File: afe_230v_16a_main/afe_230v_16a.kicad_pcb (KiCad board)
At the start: 2 copper layers, 67.7 x 86.4 mm, 1 part

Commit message: began PCBA layout
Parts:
- removed REF**: BlackPill, STM-32:YAAJ_BlackPill_SWD_1
- added C1: 1nF, Capacitor_SMD:C_0402_1005Metric, F.Cu at (157.5, 113.8)
- added C2: 1nF, Capacitor_SMD:C_0402_1005Metric, F.Cu at (173.7, 113.8)
- added D1: PDZ36B, Diode_SMD:D_SOD-323F, F.Cu at (124.4, 73.0)
- added D2: PDZ36B, Diode_SMD:D_SOD-323F, F.Cu at (121.4, 73.0)
- added D3: PDZ36B, Diode_SMD:D_SOD-323F, F.Cu at (124.9, 78.2)
- added D4: PDZ36B, Diode_SMD:D_SOD-323F, F.Cu at (121.9, 78.2)
- added J1: ~, Connector_Phoenix_MSTB:PhoenixContact_MSTBVA_2,5_2-G-5,08_1x02_P5.08mm_Vertical, F.Cu at (158.5, 134.4)
- added J2: ~, Connector_Phoenix_MSTB:PhoenixContact_MSTBVA_2,5_2-G-5,08_1x02_P5.08mm_Vertical, F.Cu at (122.6, 134.2)
- added J3: ~, Connector_Phoenix_MSTB:PhoenixContact_MSTBVA_2,5_2-G-5,08_1x02_P5.08mm_Vertical, F.Cu at (138.8, 134.0)
- added J4: MCV 1,5/ 6-G-3,81, Connector_Phoenix_MC:PhoenixContact_MCV_1,5_6-G-3.81_1x06_P3.81mm_Vertical, F.Cu at (159.7, 57.0)
- added J5: HBUS16, Connector_PinHeader_2.54mm:PinHeader_2x09_P2.54mm_Vertical, F.Cu at (119.5, 84.3)
- added R1: 680K, Resistor_SMD:R_1206_3216Metric, F.Cu at (155.4, 124.0)
- added R10: 680K, Resistor_SMD:R_1206_3216Metric, F.Cu at (176.9, 120.3)
- added R11: 680K, Resistor_SMD:R_1206_3216Metric, F.Cu at (155.4, 120.2)
- added R12: 680K, Resistor_SMD:R_1206_3216Metric, F.Cu at (171.8, 120.3)
- added R13: 499K, Resistor_SMD:R_0805_2012Metric, F.Cu at (154.8, 118.0)
- added R14: 499K, Resistor_SMD:R_0805_2012Metric, F.Cu at (171.2, 117.8)
- added R15: 20K, Resistor_SMD:R_0805_2012Metric, F.Cu at (154.4, 115.0)
- added R16: 20K, Resistor_SMD:R_0805_2012Metric, F.Cu at (170.8, 115.0)
- added R17: 20K, Resistor_SMD:R_0805_2012Metric, F.Cu at (157.5, 115.8)
- added R18: 20K, Resistor_SMD:R_0805_2012Metric, F.Cu at (173.8, 115.7)
- added R19: 0K, Resistor_SMD:R_0805_2012Metric, F.Cu at (161.7, 110.8)
- added R2: 680K, Resistor_SMD:R_1206_3216Metric, F.Cu at (171.9, 124.0)
- added R20: 1K_dnp, Resistor_SMD:R_0805_2012Metric, F.Cu at (166.3, 112.0)
- added R21: 0K, Resistor_SMD:R_0805_2012Metric, F.Cu at (178.2, 110.9)
- added R22: 33R2, Resistor_SMD:R_0805_2012Metric, F.Cu at (153.8, 108.7)
- added R23: 33R2, Resistor_SMD:R_0805_2012Metric, F.Cu at (170.3, 108.8)
- added R24: 1K_dnp, Resistor_SMD:R_0805_2012Metric, F.Cu at (163.6, 103.8)
- added R25: 1K_dnp, Resistor_SMD:R_0805_2012Metric, F.Cu at (165.8, 103.8)
- added R26: 1K_dnp, Resistor_SMD:R_0805_2012Metric, F.Cu at (170.6, 99.6)
- added R27: 1K_dnp, Resistor_SMD:R_0805_2012Metric, F.Cu at (159.2, 103.7)
- added R28: 1K_dnp, Resistor_SMD:R_0805_2012Metric, F.Cu at (159.2, 99.6)
- added R29: 0R005, Resistor_SMD:R_2512_6332Metric_Pad1.40x3.35mm_HandSolder, F.Cu at (141.4, 123.4)
- added R3: 680K, Resistor_SMD:R_1206_3216Metric, F.Cu at (160.5, 124.0)
- added R30: 1KR, Resistor_SMD:R_0805_2012Metric, F.Cu at (135.1, 115.3)
- added R31: 1KR, Resistor_SMD:R_0805_2012Metric, F.Cu at (146.5, 115.3)
- added R32: 1KR, Resistor_SMD:R_0805_2012Metric, F.Cu at (135.1, 111.5)
- added R33: 1KR, Resistor_SMD:R_0805_2012Metric, F.Cu at (146.5, 110.8)
- added R34: 1KR, Resistor_SMD:R_0805_2012Metric, F.Cu at (146.4, 106.3)
- added R35: 20K, Resistor_SMD:R_0805_2012Metric, F.Cu at (139.2, 97.8)
- added R36: 20K, Resistor_SMD:R_0805_2012Metric, F.Cu at (142.8, 97.8)
- added R37: 1KR, Resistor_SMD:R_0805_2012Metric, F.Cu at (147.1, 103.4)
- added R38: 0K_dnp, Resistor_SMD:R_0805_2012Metric, F.Cu at (144.0, 102.7)
- added R4: 680K, Resistor_SMD:R_1206_3216Metric, F.Cu at (176.9, 124.0)
- added R5: 680K, Resistor_SMD:R_1206_3216Metric, F.Cu at (165.6, 124.0)
- added R6: 680K, Resistor_SMD:R_1206_3216Metric, F.Cu at (182.0, 124.1)
- added R7: 680K, Resistor_SMD:R_1206_3216Metric, F.Cu at (165.5, 120.3)
- added R8: 680K, Resistor_SMD:R_1206_3216Metric, F.Cu at (182.0, 120.3)
- added R9: 680K, Resistor_SMD:R_1206_3216Metric, F.Cu at (160.5, 120.2)
- added U1: ~, Package_TO_SOT_SMD:TSOT-23-5, F.Cu at (157.5, 110.8)
- added U2: AD8538, Package_TO_SOT_SMD:TSOT-23-5, F.Cu at (174.2, 110.9)
- added U3: AD8538_dnp, Package_TO_SOT_SMD:TSOT-23-5, F.Cu at (164.7, 99.8)
- added U4: AQH3223A, Package_SO:SSO-7-8_6.4x9.78mm_P2.54mm, F.Cu at (125.5, 119.7)
- added U5: ACS711xLCTR-25AB, Package_SO:SOIC-8_3.9x4.9mm_P1.27mm, F.Cu at (141.2, 115.0)
- added U6: AD8538_dnp, Package_TO_SOT_SMD:TSOT-23-5, F.Cu at (140.5, 108.5)
- added U7: REF3030, Package_TO_SOT_SMD:SOT-23, F.Cu at (135.2, 103.9)
- added U9: YAAJ_BlackPill, STM-32:YAAJ_BlackPill_SWD_2, F.Cu at (90.1, 76.5)
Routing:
- net (no net): vias 0 -> 10

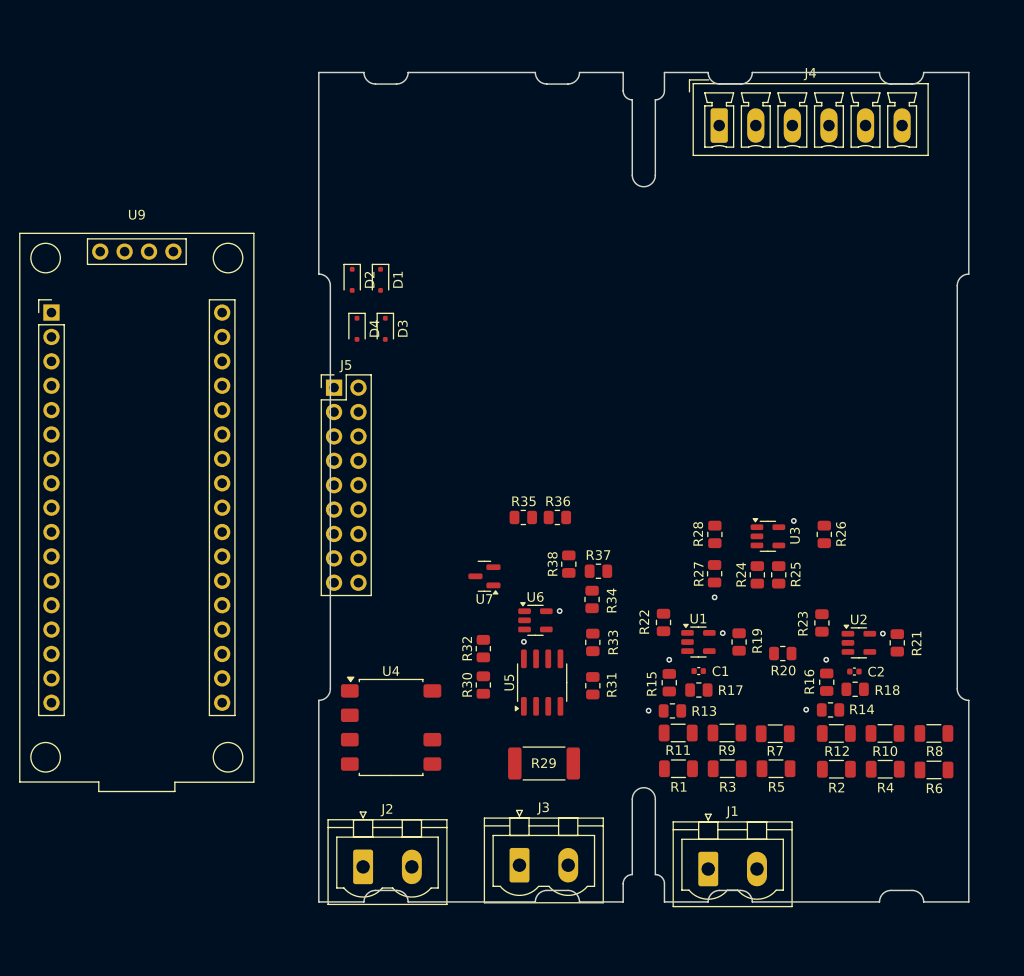
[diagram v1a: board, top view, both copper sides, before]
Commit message: alternate layout
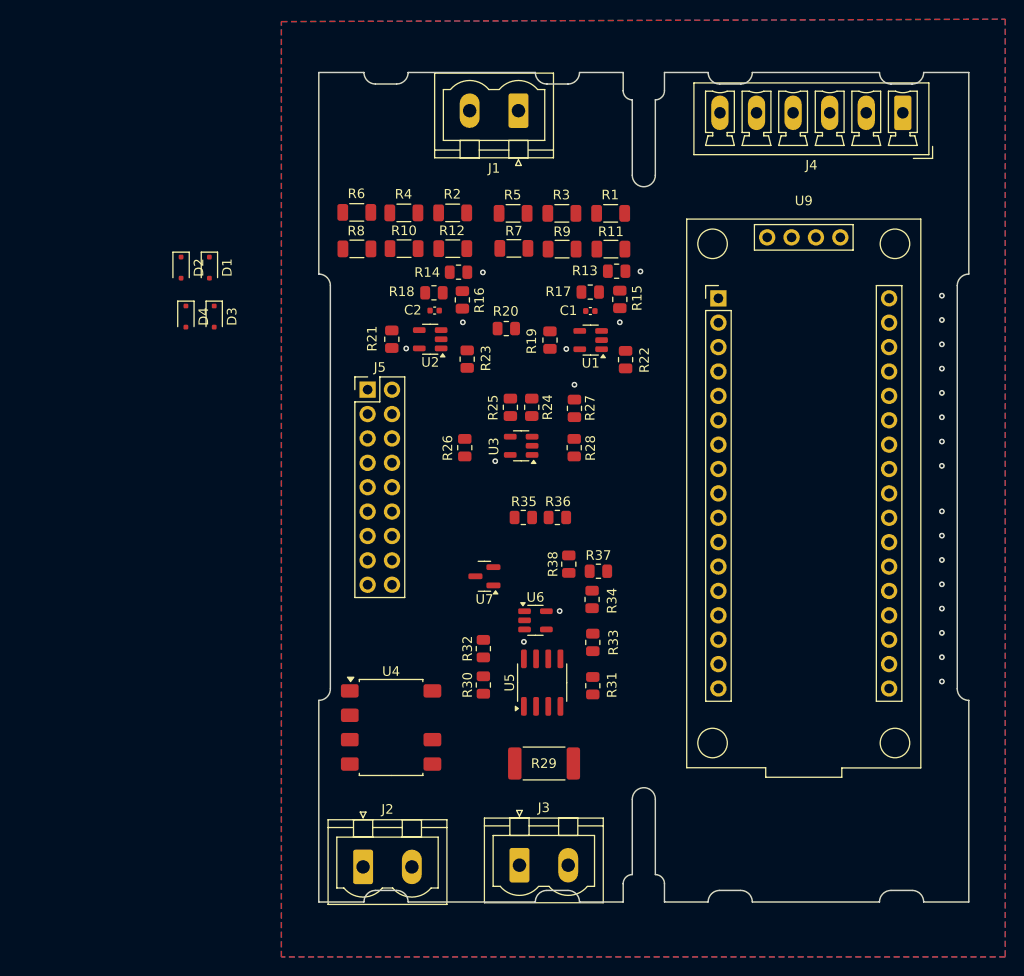
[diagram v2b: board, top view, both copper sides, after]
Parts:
- moved R6 83.6 mm to (121.9, 66.0), turned to 180 degrees
- moved J1 81.4 mm to (138.7, 55.4), turned to 180 degrees
- moved R8 78.5 mm to (121.9, 69.8), turned to 0 degrees
- moved R4 76.6 mm to (126.8, 66.1), turned to 180 degrees
- moved R10 71.1 mm to (126.8, 69.8), turned to 0 degrees
- moved R2 70.4 mm to (131.9, 66.1), turned to 180 degrees
- moved U9 69.5 mm to (159.6, 75.0)
- moved R12 64.4 mm to (131.9, 69.8), turned to 0 degrees
- moved R5 64.0 mm to (138.2, 66.1), turned to 180 degrees
- moved R21 61.4 mm to (125.5, 79.2), turned to 90 degrees
- moved R3 60.4 mm to (143.3, 66.1), turned to 180 degrees
- moved R18 60.3 mm to (129.9, 74.4), turned to 0 degrees
- moved R14 59.8 mm to (132.5, 72.2), turned to 180 degrees
- moved R1 58.3 mm to (148.3, 66.1), turned to 180 degrees
- moved C2 57.7 mm to (130.0, 76.2), turned to 180 degrees
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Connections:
- J5 pad 10: /K1_on -> unconnected-(J5-Pin_10-Pad10)
- J5 pad 11: /CAN_lo -> /CAN_hi
- J5 pad 12: /K1_status -> /K1_on
- J5 pad 13: /24V -> /CAN_lo
- J5 pad 14: /K2_on -> /K1_status
- J5 pad 15: /DGND -> /24V
- J5 pad 16: /K2_status -> /K2_on
- J5 pad 17: (no net) -> /DGND
- J5 pad 18: (no net) -> /K2_status
- J5 pad 9: /CAN_hi -> unconnected-(J5-Pin_9-Pad9)
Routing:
- net Earth: vias 0 -> 16
- added copper zone on B.Cu, net Earth
- added copper zone on F.Cu, net Earth
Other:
- board text added: "I p/n"
- board text added: "K i/o"
- board text added: "V p/n"
- board text added: "blackpill i/o"
- board text added: "outputs & pwr/gnd in"

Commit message: added pcb2&3 board outlines, adjusted i/o
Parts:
- added J6: pinheader_1x6, Connector_PinHeader_2.54mm:PinHeader_1x06_P2.54mm_Vertical, F.Cu at (164.0, 132.4)
- added J6: pinheader_1x6, Connector_PinHeader_2.54mm:PinHeader_1x06_P2.54mm_Vertical, F.Cu at (166.7, 80.8)
- added J6: pinheader_1x6, Connector_PinHeader_2.54mm:PinHeader_1x06_P2.54mm_Vertical, F.Cu at (247.8, 87.5)
- D1, D2, D3, D4: footprint Diode_SMD:D_SOD-323F -> Diode_SMD:D_SOD-323_HandSoldering
- moved J2 90.7 mm to (167.7, 55.5)
- moved J1 79.8 mm to (124.9, 134.0), turned to 0 degrees
- moved U9 68.0 mm to (214.7, 114.9), turned to 90 degrees
- moved U4 67.8 mm to (171.3, 69.7), turned to 90 degrees
- moved R6 65.8 mm to (160.9, 119.0), turned to 0 degrees
- moved R4 60.4 mm to (155.9, 119.0), turned to 0 degrees
- moved R8 59.9 mm to (160.9, 115.3), turned to 180 degrees
- moved R2 56.3 mm to (150.9, 119.0), turned to 0 degrees
- moved R1 54.7 mm to (134.4, 119.0), turned to 0 degrees
- moved J4 54.1 mm to (124.7, 57.2), turned to 0 degrees
- moved R10 54.0 mm to (155.9, 115.3), turned to 180 degrees
- moved R5 53.3 mm to (144.6, 119.0), turned to 0 degrees
- moved R3 53.0 mm to (139.5, 119.0), turned to 0 degrees
- moved R12 49.3 mm to (150.9, 115.3), turned to 180 degrees
- moved R11 47.5 mm to (134.4, 115.3), turned to 180 degrees
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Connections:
- U9 pad 23: unconnected-(U9-PA0-Pad23) -> /A0
- U9 pad 24: unconnected-(U9-PA1-Pad24) -> /A1
- U9 pad 25: unconnected-(U9-PA2-Pad25) -> /A2
- U9 pad 31: unconnected-(U9-PB0-Pad31) -> /D0
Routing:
- net /V0_sense: track 0.00 -> 1.67 mm, vias 0 -> 1
- net /V1_sense: track 0.00 -> 1.52 mm, vias 0 -> 1
- net /A2: vias 0 -> 1
- net /3V3: vias 0 -> 6
- net /3V0_REF: vias 0 -> 4
- net /1V5_REF: vias 0 -> 3
- net (no net): vias 10 -> 0
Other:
- board size 67.7 x 86.4 mm -> 238.4 x 117.6 mm
- board text added: "pcb2 BC71,6 UT-11' 3,55 clearance"
- board text added: "pcb3 BC71,6 UT-11' 8,6 clearance"
- board text added: "pwr/gnd in & outputs"
- board text removed: "outputs & pwr/gnd in"

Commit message: pleased with layout, onto wiring
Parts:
- moved R31 38.6 mm to (156.3, 114.5), turned to -90 degrees
- moved R29 38.1 mm to (150.6, 118.8), turned to 0 degrees
- moved R33 35.2 mm to (156.3, 110.8), turned to 90 degrees
- moved R34 31.7 mm to (156.2, 106.3), turned to 90 degrees
- moved U5 31.1 mm to (151.0, 112.3), turned to 90 degrees
- moved R35 28.3 mm to (146.9, 99.8), turned to 180 degrees
- moved R38 27.5 mm to (155.3, 101.9)
- moved U7 27.2 mm to (142.0, 100.7)
- moved R36 26.7 mm to (150.7, 99.8), turned to 180 degrees
- moved R6 25.8 mm to (135.2, 117.8)
- moved R8 25.7 mm to (135.2, 115.3)
- moved R30 24.9 mm to (145.5, 111.0), turned to 90 degrees
- moved R24 24.8 mm to (139.2, 74.1)
- moved R25 24.8 mm to (141.4, 74.1)
- moved U3 24.8 mm to (140.2, 70.1)
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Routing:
- net /V1_sense: track 1.52 -> 13.2 mm
- net /V0_sense: track 1.67 -> 4.02 mm
- net /I0_sense: track 0.00 -> 1.53 mm, vias 0 -> 1
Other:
- board size 238.4 x 117.6 mm -> 342.7 x 117.6 mm
